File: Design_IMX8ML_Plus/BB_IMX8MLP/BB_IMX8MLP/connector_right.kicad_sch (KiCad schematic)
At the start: 2 parts, among them J1 DF40C-80DP-0.4V_51_, J2 Front_Right

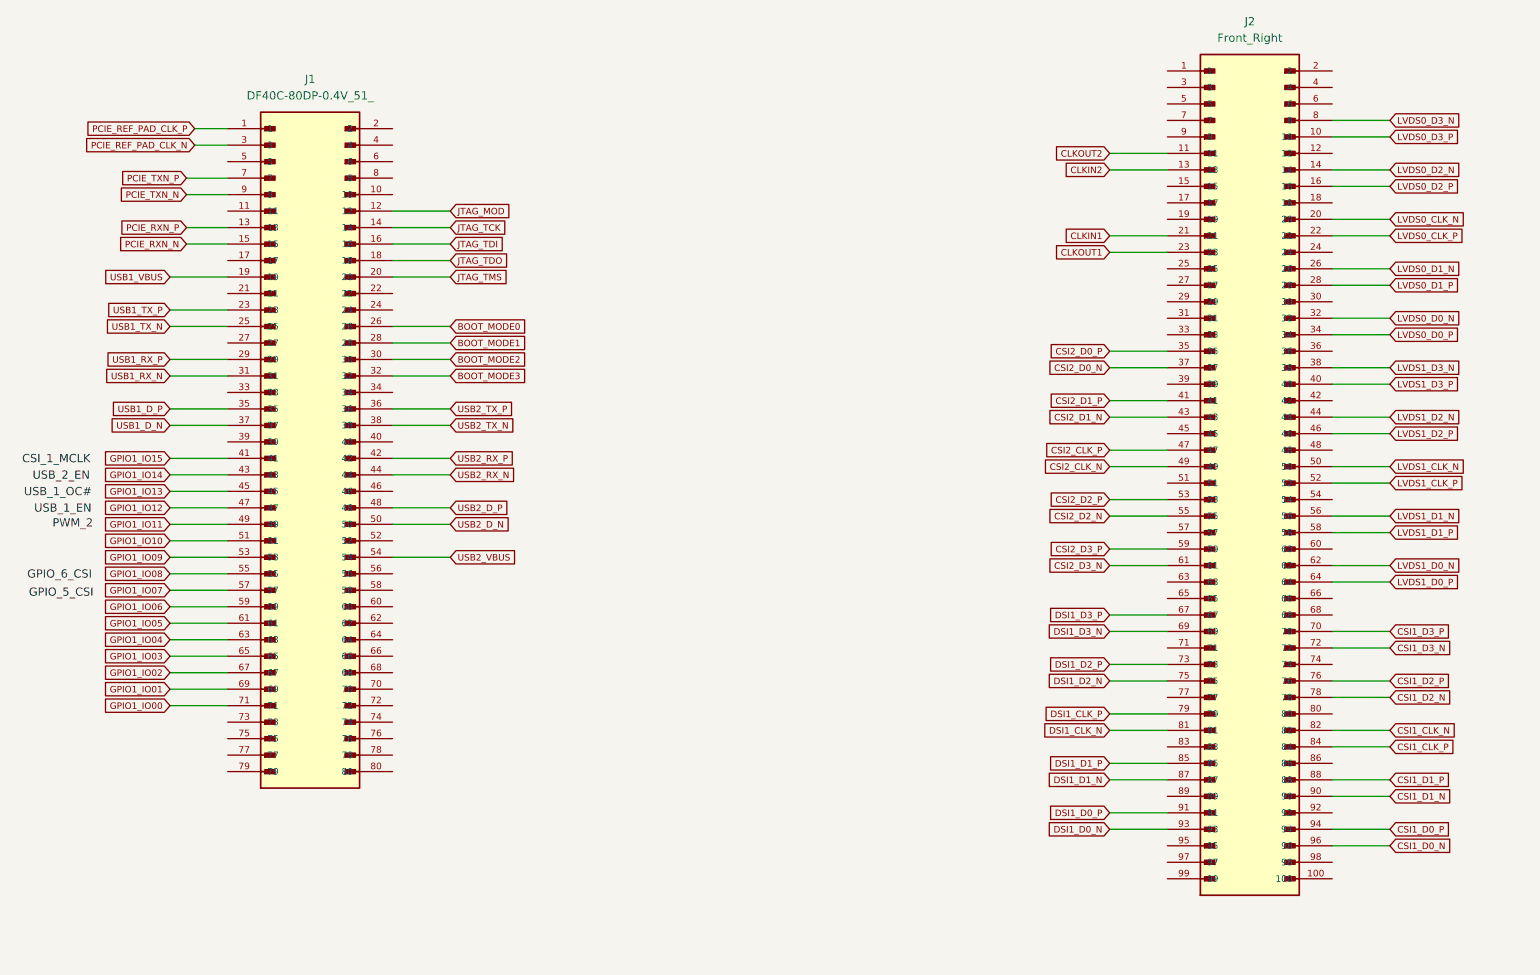
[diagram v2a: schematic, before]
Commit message: [BB_IMX8MLP IMX8MLP] Actuallizated to 9.0 kicad version
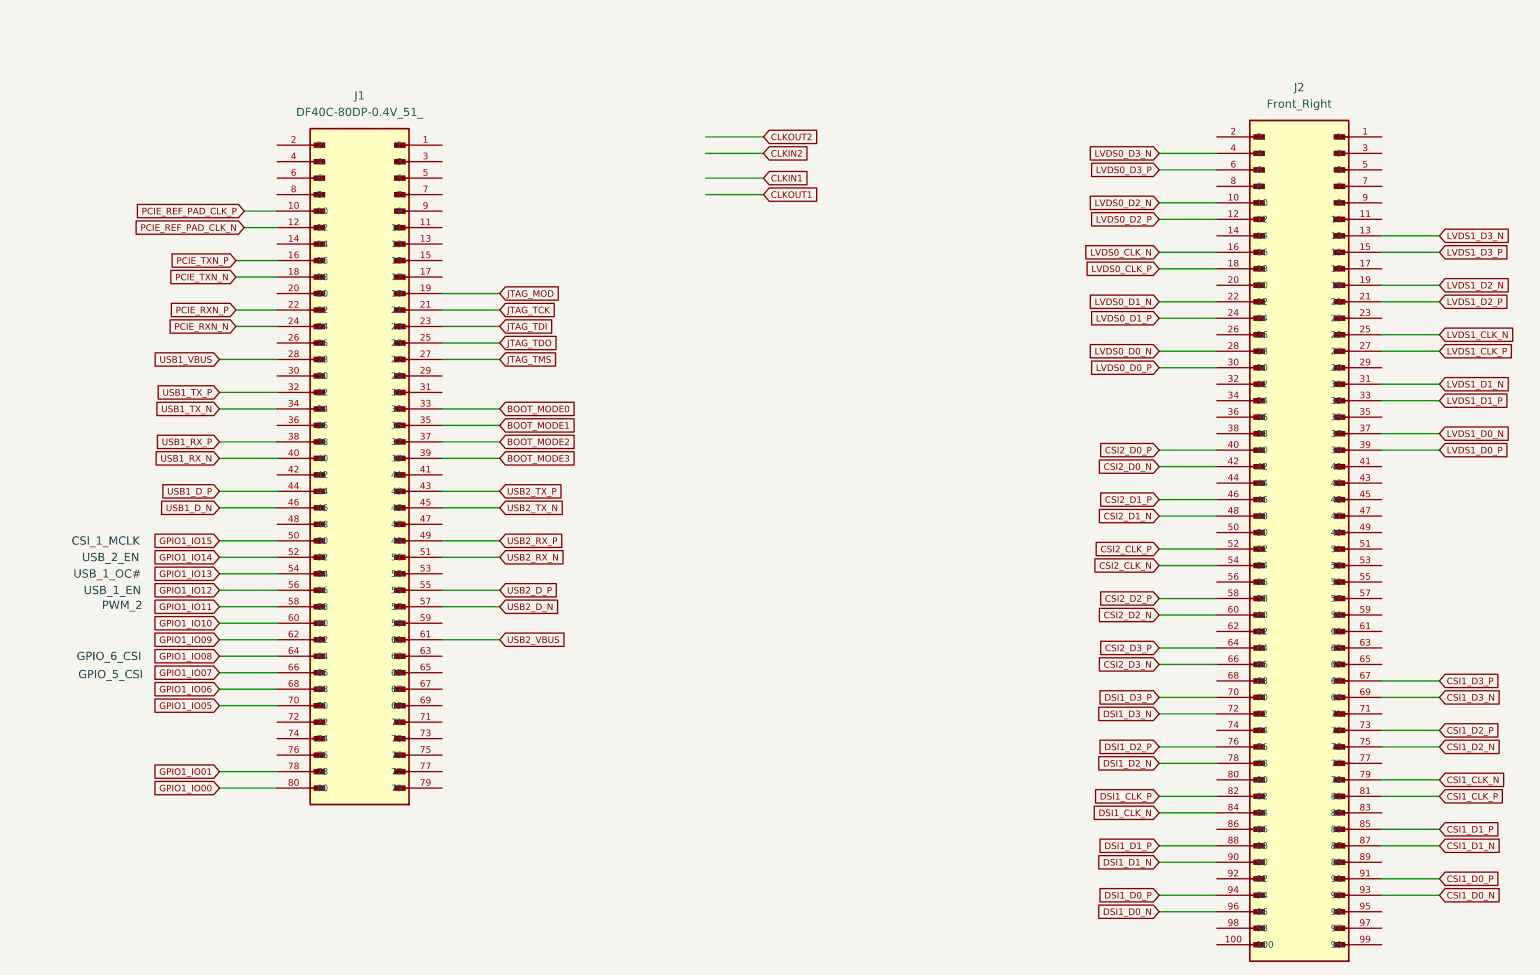
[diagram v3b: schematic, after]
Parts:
- J1: footprint _W_SBC:HRS_DF40C-80DS-0.4V_51_ -> _W_SBC:HRS_DF40C-80DP-0.4V_51_; Price None -> 2
- J2: footprint _W_SBC:HIROSE_DF40C-100DS-0.4V_51_ -> _W_SBC:HRS_DF40C-100DP-0.4V_51_; Price None -> 2
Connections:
- net BOOT_MODE0: now also J1.33; no longer J1.26
- net BOOT_MODE1: now also J1.35; no longer J1.28
- net BOOT_MODE2: now also J1.37; no longer J1.30
- net BOOT_MODE3: now also J1.39; no longer J1.32
- net CLKIN1: no longer J2.21
- net CLKIN2: no longer J2.13
- net CLKOUT1: no longer J2.23
- net CLKOUT2: no longer J2.11
- net CSI1_CLK_N: now also J2.79; no longer J2.82
- net CSI1_CLK_P: now also J2.81; no longer J2.84
- net CSI1_D0_N: now also J2.93; no longer J2.96
- net CSI1_D0_P: now also J2.91; no longer J2.94
- net CSI1_D1_N: now also J2.87; no longer J2.90
- net CSI1_D1_P: now also J2.85; no longer J2.88
- net CSI1_D2_N: now also J2.75; no longer J2.78
- net CSI1_D2_P: now also J2.73; no longer J2.76
- net CSI1_D3_N: now also J2.69; no longer J2.72
- net CSI1_D3_P: now also J2.67; no longer J2.70
- net CSI2_CLK_N: now also J2.54; no longer J2.49
- net CSI2_CLK_P: now also J2.52; no longer J2.47
- net CSI2_D0_N: now also J2.42; no longer J2.37
- net CSI2_D0_P: now also J2.40; no longer J2.35
- net CSI2_D1_N: now also J2.48; no longer J2.43
- net CSI2_D1_P: now also J2.46; no longer J2.41
- net CSI2_D2_N: now also J2.60; no longer J2.55
- net CSI2_D2_P: now also J2.58; no longer J2.53
- net CSI2_D3_N: now also J2.66; no longer J2.61
- net CSI2_D3_P: now also J2.64; no longer J2.59
- net DSI1_CLK_N: now also J2.84; no longer J2.81
- net DSI1_CLK_P: now also J2.82; no longer J2.79
- net DSI1_D0_N: now also J2.96; no longer J2.93
- net DSI1_D0_P: now also J2.94; no longer J2.91
- net DSI1_D1_N: now also J2.90; no longer J2.87
- net DSI1_D1_P: now also J2.88; no longer J2.85
- net DSI1_D2_N: now also J2.78; no longer J2.75
- net DSI1_D2_P: now also J2.76; no longer J2.73
- net DSI1_D3_N: now also J2.72; no longer J2.69
- net DSI1_D3_P: now also J2.70; no longer J2.67
- net GPIO1_IO00: now also J1.80; no longer J1.71
- net GPIO1_IO01: now also J1.78; no longer J1.69
- net GPIO1_IO05: now also J1.70; no longer J1.61
- net GPIO1_IO06: now also J1.68; no longer J1.59
- net GPIO1_IO07: now also J1.66; no longer J1.57
- net GPIO1_IO08: now also J1.64; no longer J1.55
- net GPIO1_IO09: now also J1.62; no longer J1.53
- net GPIO1_IO10: now also J1.60; no longer J1.51
- net GPIO1_IO11: now also J1.58; no longer J1.49
- net GPIO1_IO12: now also J1.56; no longer J1.47
- net GPIO1_IO13: now also J1.54; no longer J1.45
- net GPIO1_IO14: now also J1.52; no longer J1.43
- net GPIO1_IO15: now also J1.50; no longer J1.41
- net JTAG_MOD: now also J1.19; no longer J1.12
- net JTAG_TCK: now also J1.21; no longer J1.14
- net JTAG_TDI: now also J1.23; no longer J1.16
- net JTAG_TDO: now also J1.25; no longer J1.18
- net JTAG_TMS: now also J1.27; no longer J1.20
- net LVDS0_CLK_N: now also J2.16; no longer J2.20
- net LVDS0_CLK_P: now also J2.18; no longer J2.22
- net LVDS0_D0_N: now also J2.28; no longer J2.32
- net LVDS0_D0_P: now also J2.30; no longer J2.34
- net LVDS0_D1_N: now also J2.22; no longer J2.26
- net LVDS0_D1_P: now also J2.24; no longer J2.28
- net LVDS0_D2_N: now also J2.10; no longer J2.14
- net LVDS0_D2_P: now also J2.12; no longer J2.16
- net LVDS0_D3_N: now also J2.4; no longer J2.8
- net LVDS0_D3_P: now also J2.6; no longer J2.10
- net LVDS1_CLK_N: now also J2.25; no longer J2.50
- net LVDS1_CLK_P: now also J2.27; no longer J2.52
- net LVDS1_D0_N: now also J2.37; no longer J2.62
- net LVDS1_D0_P: now also J2.39; no longer J2.64
- net LVDS1_D1_N: now also J2.31; no longer J2.56
- net LVDS1_D1_P: now also J2.33; no longer J2.58
- net LVDS1_D2_N: now also J2.19; no longer J2.44
- net LVDS1_D2_P: now also J2.21; no longer J2.46
- net LVDS1_D3_N: now also J2.13; no longer J2.38
- net LVDS1_D3_P: now also J2.15; no longer J2.40
- net PCIE_REF_PAD_CLK_N: now also J1.12; no longer J1.3
- net PCIE_REF_PAD_CLK_P: now also J1.10; no longer J1.1
- net PCIE_RXN_N: now also J1.24; no longer J1.15
- net PCIE_RXN_P: now also J1.22; no longer J1.13
- net PCIE_TXN_N: now also J1.18; no longer J1.9
- net PCIE_TXN_P: now also J1.16; no longer J1.7
- net USB1_D_N: now also J1.46; no longer J1.37
- net USB1_D_P: now also J1.44; no longer J1.35
- net USB1_RX_N: now also J1.40; no longer J1.31
- net USB1_RX_P: now also J1.38; no longer J1.29
- net USB1_TX_N: now also J1.34; no longer J1.25
- net USB1_TX_P: now also J1.32; no longer J1.23
- net USB1_VBUS: now also J1.28; no longer J1.19
- net USB2_D_N: now also J1.57; no longer J1.50
- net USB2_D_P: now also J1.55; no longer J1.48
- net USB2_RX_N: now also J1.51; no longer J1.44
- net USB2_RX_P: now also J1.49; no longer J1.42
- net USB2_TX_N: now also J1.45; no longer J1.38
- net USB2_TX_P: now also J1.43; no longer J1.36
- net USB2_VBUS: now also J1.61; no longer J1.54
- net GPIO1_IO02: no longer names the net of J1.67
- net GPIO1_IO03: no longer names the net of J1.65
- net GPIO1_IO04: no longer names the net of J1.63
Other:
- moved on the sheet: J1, J2

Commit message: [IMX8ML] Add new layer
A new layers was add in the cpu schematic, now it had 8 layer.
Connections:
- net CSI1_CLK_N: now also J2.18; no longer J2.79
- net CSI1_CLK_P: now also J2.20; no longer J2.81
- net CSI1_D0_N: now also J2.32; no longer J2.93
- net CSI1_D0_P: now also J2.30; no longer J2.91
- net CSI1_D1_N: now also J2.26; no longer J2.87
- net CSI1_D1_P: now also J2.24; no longer J2.85
- net CSI1_D2_N: now also J2.14; no longer J2.75
- net CSI1_D2_P: now also J2.12; no longer J2.73
- net CSI1_D3_N: now also J2.8; no longer J2.69
- net CSI1_D3_P: now also J2.6; no longer J2.67
- net LVDS0_CLK_N: now also J2.59; no longer J2.16
- net LVDS0_CLK_P: now also J2.61; no longer J2.18
- net LVDS0_D0_N: now also J2.71; no longer J2.28
- net LVDS0_D0_P: now also J2.73; no longer J2.30
- net LVDS0_D1_N: now also J2.65; no longer J2.22
- net LVDS0_D1_P: now also J2.67; no longer J2.24
- net LVDS0_D2_N: now also J2.53; no longer J2.10
- net LVDS0_D2_P: now also J2.55; no longer J2.12
- net LVDS0_D3_N: now also J2.47; no longer J2.4
- net LVDS0_D3_P: now also J2.49; no longer J2.6
- net LVDS1_CLK_N: now also J2.23; no longer J2.25
- net LVDS1_CLK_P: now also J2.25; no longer J2.27
- net LVDS1_D0_N: now also J2.35; no longer J2.37
- net LVDS1_D0_P: now also J2.37; no longer J2.39
- net LVDS1_D1_N: now also J2.29; no longer J2.31
- net LVDS1_D1_P: now also J2.31; no longer J2.33
- net LVDS1_D2_N: now also J2.17; no longer J2.19
- net LVDS1_D2_P: now also J2.19; no longer J2.21
- net LVDS1_D3_N: now also J2.11; no longer J2.13
- net LVDS1_D3_P: now also J2.13; no longer J2.15
- net CTRL_RESET_MOCI: now reaches J2.89
- new net ON/OFF: J2.85
- new net PMIC_RST_B: J2.87
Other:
- note added: "ON/OFF Processor POR_B PMIC/Processor PMIC_RST_B PMIC PMIC_ON_REQ PMIC/Processor WDOG_B PMIC/Processor"
